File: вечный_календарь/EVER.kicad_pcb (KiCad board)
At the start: 2 copper layers, 79.8 x 65.6 mm, 44 parts, among them U1 YAAJ_DCDC_StepUp_SX1308, U2 ESP32-H2-DEVKITM-1-N4

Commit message: endless_calendar: минорное изменение
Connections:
- U1 pad 2: -BATT -> Net-(U2-GND_J3_1)
- U1 pad 3: Net-(U2-GND_J3_10) -> -BATT
- U2 pad J3_1: -BATT -> Net-(U2-GND_J3_1)
- U2 pad J3_10: Net-(U2-GND_J3_10) -> unconnected-(U2-GND_J3_10-PadJ3_10)
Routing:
- net Net-(U2-GND_J3_10): track 27.4 -> 0.00 mm
- net (no net): track 0.00 -> 27.4 mm
- net Net-(U2-GND_J3_1): track 0.00 -> 14.0 mm
- net -BATT: track 14.0 -> 0.00 mm

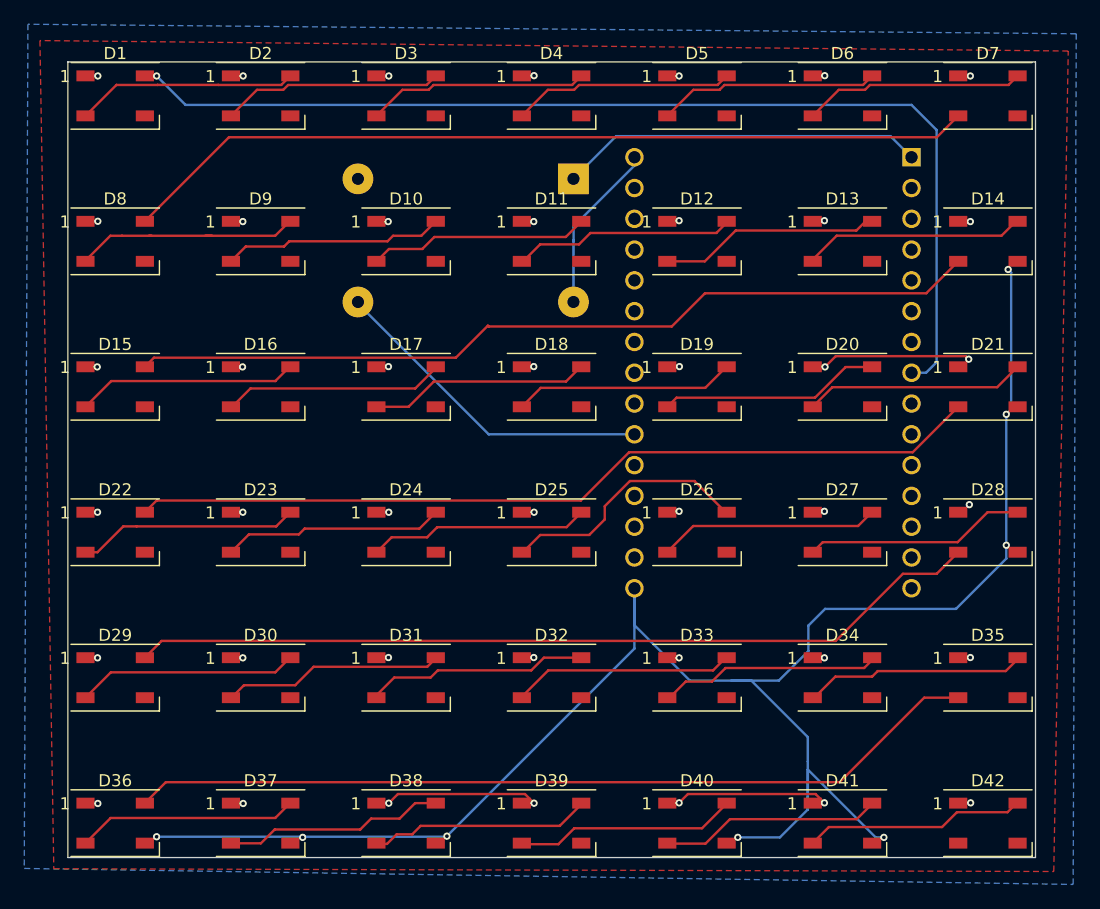
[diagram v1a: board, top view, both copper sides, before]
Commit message: endless_calendar: h2 -> s3 devkit; resistors added; added example for arduino code
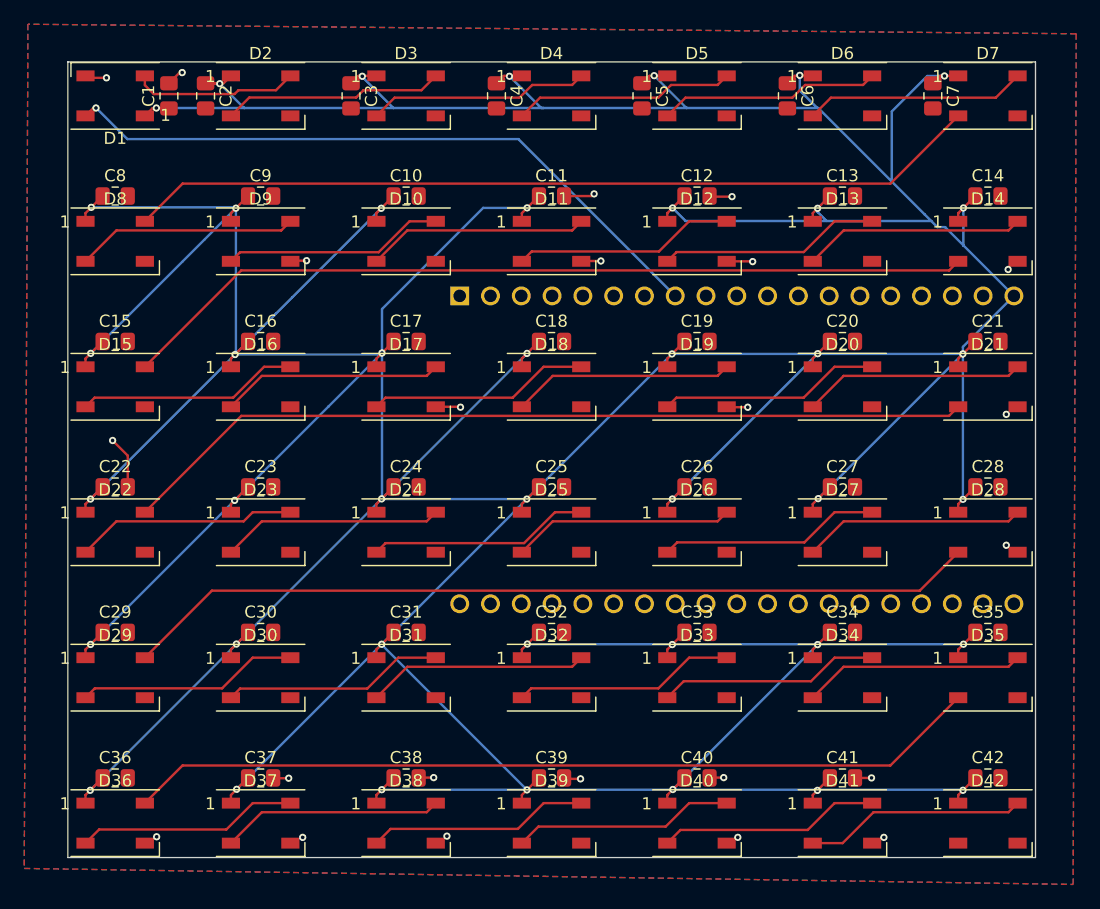
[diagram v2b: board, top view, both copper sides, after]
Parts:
- removed U1: YAAJ_DCDC_StepUp_SX1308, dcdc_stepup_sx1308:YAAJ_DCDC_StepUp_SX1308
- added C1: 100n, Capacitor_SMD:C_0805_2012Metric_Pad1.18x1.45mm_HandSolder, F.Cu at (109.0, 27.6)
- added C10: 100n, Capacitor_SMD:C_0805_2012Metric_Pad1.18x1.45mm_HandSolder, F.Cu at (128.6, 35.8)
- added C11: 100n, Capacitor_SMD:C_0805_2012Metric_Pad1.18x1.45mm_HandSolder, F.Cu at (140.6, 35.8)
- added C12: 100n, Capacitor_SMD:C_0805_2012Metric_Pad1.18x1.45mm_HandSolder, F.Cu at (152.6, 35.8)
- added C13: 100n, Capacitor_SMD:C_0805_2012Metric_Pad1.18x1.45mm_HandSolder, F.Cu at (164.6, 35.8)
- added C14: 100n, Capacitor_SMD:C_0805_2012Metric_Pad1.18x1.45mm_HandSolder, F.Cu at (176.6, 35.8)
- added C15: 100n, Capacitor_SMD:C_0805_2012Metric_Pad1.18x1.45mm_HandSolder, F.Cu at (104.6, 47.8)
- added C16: 100n, Capacitor_SMD:C_0805_2012Metric_Pad1.18x1.45mm_HandSolder, F.Cu at (116.6, 47.8)
- added C17: 100n, Capacitor_SMD:C_0805_2012Metric_Pad1.18x1.45mm_HandSolder, F.Cu at (128.6, 47.8)
- added C18: 100n, Capacitor_SMD:C_0805_2012Metric_Pad1.18x1.45mm_HandSolder, F.Cu at (140.6, 47.8)
- added C19: 100n, Capacitor_SMD:C_0805_2012Metric_Pad1.18x1.45mm_HandSolder, F.Cu at (152.6, 47.8)
- added C2: 100n, Capacitor_SMD:C_0805_2012Metric_Pad1.18x1.45mm_HandSolder, F.Cu at (112.0, 27.6)
- added C20: 100n, Capacitor_SMD:C_0805_2012Metric_Pad1.18x1.45mm_HandSolder, F.Cu at (164.6, 47.8)
- added C21: 100n, Capacitor_SMD:C_0805_2012Metric_Pad1.18x1.45mm_HandSolder, F.Cu at (176.6, 47.8)
- added C22: 100n, Capacitor_SMD:C_0805_2012Metric_Pad1.18x1.45mm_HandSolder, F.Cu at (104.6, 59.8)
- added C23: 100n, Capacitor_SMD:C_0805_2012Metric_Pad1.18x1.45mm_HandSolder, F.Cu at (116.6, 59.8)
- added C24: 100n, Capacitor_SMD:C_0805_2012Metric_Pad1.18x1.45mm_HandSolder, F.Cu at (128.6, 59.8)
- added C25: 100n, Capacitor_SMD:C_0805_2012Metric_Pad1.18x1.45mm_HandSolder, F.Cu at (140.6, 59.8)
- added C26: 100n, Capacitor_SMD:C_0805_2012Metric_Pad1.18x1.45mm_HandSolder, F.Cu at (152.6, 59.8)
- added C27: 100n, Capacitor_SMD:C_0805_2012Metric_Pad1.18x1.45mm_HandSolder, F.Cu at (164.6, 59.8)
- added C28: 100n, Capacitor_SMD:C_0805_2012Metric_Pad1.18x1.45mm_HandSolder, F.Cu at (176.6, 59.8)
- added C29: 100n, Capacitor_SMD:C_0805_2012Metric_Pad1.18x1.45mm_HandSolder, F.Cu at (104.6, 71.8)
- added C3: 100n, Capacitor_SMD:C_0805_2012Metric_Pad1.18x1.45mm_HandSolder, F.Cu at (124.0, 27.6)
- added C30: 100n, Capacitor_SMD:C_0805_2012Metric_Pad1.18x1.45mm_HandSolder, F.Cu at (116.6, 71.8)
- added C31: 100n, Capacitor_SMD:C_0805_2012Metric_Pad1.18x1.45mm_HandSolder, F.Cu at (128.6, 71.8)
- added C32: 100n, Capacitor_SMD:C_0805_2012Metric_Pad1.18x1.45mm_HandSolder, F.Cu at (140.6, 71.8)
- added C33: 100n, Capacitor_SMD:C_0805_2012Metric_Pad1.18x1.45mm_HandSolder, F.Cu at (152.6, 71.8)
- added C34: 100n, Capacitor_SMD:C_0805_2012Metric_Pad1.18x1.45mm_HandSolder, F.Cu at (164.6, 71.8)
- added C35: 100n, Capacitor_SMD:C_0805_2012Metric_Pad1.18x1.45mm_HandSolder, F.Cu at (176.6, 71.8)
- added C36: 100n, Capacitor_SMD:C_0805_2012Metric_Pad1.18x1.45mm_HandSolder, F.Cu at (104.6, 83.8)
- added C37: 100n, Capacitor_SMD:C_0805_2012Metric_Pad1.18x1.45mm_HandSolder, F.Cu at (116.6, 83.8)
- added C38: 100n, Capacitor_SMD:C_0805_2012Metric_Pad1.18x1.45mm_HandSolder, F.Cu at (128.6, 83.8)
- added C39: 100n, Capacitor_SMD:C_0805_2012Metric_Pad1.18x1.45mm_HandSolder, F.Cu at (140.6, 83.8)
- added C4: 100n, Capacitor_SMD:C_0805_2012Metric_Pad1.18x1.45mm_HandSolder, F.Cu at (136.0, 27.6)
- added C40: 100n, Capacitor_SMD:C_0805_2012Metric_Pad1.18x1.45mm_HandSolder, F.Cu at (152.6, 83.8)
- added C41: 100n, Capacitor_SMD:C_0805_2012Metric_Pad1.18x1.45mm_HandSolder, F.Cu at (164.6, 83.8)
- added C42: 100n, Capacitor_SMD:C_0805_2012Metric_Pad1.18x1.45mm_HandSolder, F.Cu at (176.6, 83.8)
- added C5: 100n, Capacitor_SMD:C_0805_2012Metric_Pad1.18x1.45mm_HandSolder, F.Cu at (148.0, 27.6)
- added C6: 100n, Capacitor_SMD:C_0805_2012Metric_Pad1.18x1.45mm_HandSolder, F.Cu at (160.0, 27.6)
- added C7: 100n, Capacitor_SMD:C_0805_2012Metric_Pad1.18x1.45mm_HandSolder, F.Cu at (172.0, 27.6)
- added C8: 100n, Capacitor_SMD:C_0805_2012Metric_Pad1.18x1.45mm_HandSolder, F.Cu at (104.6, 35.8)
- added C9: 100n, Capacitor_SMD:C_0805_2012Metric_Pad1.18x1.45mm_HandSolder, F.Cu at (116.6, 35.8)
- U2: value ESP32-H2-DEVKITM-1-N4 -> ESP32-DEVKITC-32D; footprint ESP32-H2-DEVKITM-1-N4:MODULE_ESP32-H2-DEVKITM-1-N4 -> ESP32-DEVKITC-32D:MODULE_ESP32-DEVKITC-32D
- moved U2 6.29 mm to (152.8, 56.8), turned to -90 degrees
- turned D1 to 180 degrees
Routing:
- net +5V: track 37.5 -> 702.7 mm
- net GND: track 148.8 -> 27.5 mm, vias 8 -> 23
- net /DATA: track 87.8 -> 55.3 mm
- net Net-(U1-Vin): track 30.1 -> 0.00 mm
- net (no net): track 27.4 -> 0.00 mm
- net Net-(U2-GND_J3_1): track 14.0 -> 0.00 mm
- net Net-(D1-DOUT): track 18.3 -> 13.7 mm
- net Net-(D25-DOUT): track 21.1 -> 18.3 mm
- net Net-(D8-DOUT): track 19.1 -> 18.3 mm
- added copper zone on B.Cu, net GND
- removed copper zone on B.Cu, net +5V
